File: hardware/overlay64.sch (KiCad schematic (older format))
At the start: 16 parts, among them IC1 ATMEGA328P-P, P1 ISP, P2 MAIN, P3 INPUT, Q1 BC547, U1 LM1881, Y1 20MHz

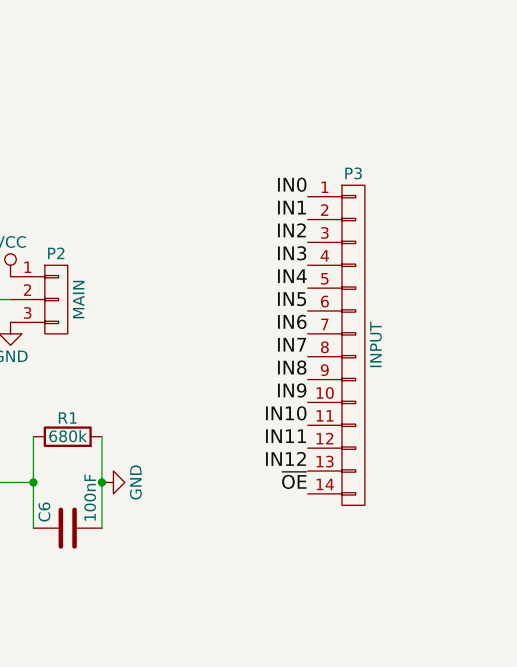
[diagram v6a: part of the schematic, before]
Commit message: Hardware: Added dual 14 pin header for bypassing the inputs
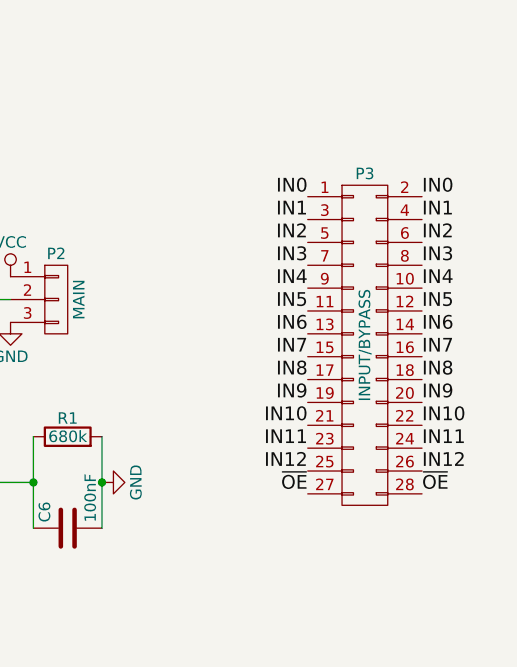
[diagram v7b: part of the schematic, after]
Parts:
- removed P3: INPUT, Pin_Headers:Pin_Header_Straight_1x14, symbol CONN_01X14
- added P3: INPUT/BYPASS, Pin_Headers:Pin_Header_Straight_2x14, symbol CONN_02X14
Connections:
- net IN0: now also P3.1 (P1), P3.2 (P2)
- net IN1: now also P3.3 (P3), P3.4 (P4)
- net IN10: now also P3.21 (P21), P3.22 (P22)
- net IN11: now also P3.23 (P23), P3.24 (P24)
- net IN12: now also P3.25 (P25), P3.26 (P26)
- net IN2: now also P3.5 (P5), P3.6 (P6)
- net IN3: now also P3.7 (P7), P3.8 (P8)
- net IN4: now also P3.10 (P10), P3.9 (P9)
- net IN5: now also P3.11 (P11), P3.12 (P12)
- net IN6: now also P3.13 (P13), P3.14 (P14)
- net IN7: now also P3.15 (P15), P3.16 (P16)
- net IN8: now also P3.17 (P17), P3.18 (P18)
- net IN9: now also P3.19 (P19), P3.20 (P20)
- net ~OE: now also P3.27 (P27), P3.28 (P28)
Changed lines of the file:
@@
 $EndComp
 $Comp
-L PWR_FLAG #FLG1
+L PWR_FLAG #FLG01
 U 1 1 56A1EF0B
 P 6250 7500
-F 0 "#FLG1" H 6250 7595 50  0001 C CNN
+F 0 "#FLG01" H 6250 7595 50  0001 C CNN
 F 1 "PWR_FLAG" H 6250 7680 50  0000 C CNN
 F 2 "" H 6250 7500 60  0000 C CNN
@@
 $EndComp
 $Comp
-L VCC #PWR12
+L VCC #PWR02
 U 1 1 56A1EF40
 P 6250 7500
-F 0 "#PWR12" H 6250 7350 50  0001 C CNN
+F 0 "#PWR02" H 6250 7350 50  0001 C CNN
 F 1 "VCC" H 6250 7650 50  0000 C CNN
 F 2 "" H 6250 7500 60  0000 C CNN
@@
 $EndComp
 $Comp
-L PWR_FLAG #FLG2
+L PWR_FLAG #FLG03
 U 1 1 56A1EF56
 P 6700 7500
-F 0 "#FLG2" H 6700 7595 50  0001 C CNN
+F 0 "#FLG03" H 6700 7595 50  0001 C CNN
 F 1 "PWR_FLAG" H 6700 7680 50  0000 C CNN
 F 2 "" H 6700 7500 60  0000 C CNN
@@
 $EndComp
 $Comp
-L GND #PWR15
+L GND #PWR04
 U 1 1 56A1EF6C
 P 6700 7500
-F 0 "#PWR15" H 6700 7250 50  0001 C CNN
+F 0 "#PWR04" H 6700 7250 50  0001 C CNN
 F 1 "GND" H 6700 7350 50  0000 C CNN
 F 2 "" H 6700 7500 60  0000 C CNN
@@
 $EndComp
 $Comp
-L VCC #PWR9
+L VCC #PWR05
 U 1 1 56A1F13D
 P 5600 4850
-F 0 "#PWR9" H 5600 4700 50  0001 C CNN
+F 0 "#PWR05" H 5600 4700 50  0001 C CNN
 F 1 "VCC" H 5600 5000 50  0000 C CNN
 F 2 "" H 5600 4850 60  0000 C CNN
@@
 $EndComp
 $Comp
-L GND #PWR10
+L GND #PWR06
 U 1 1 56A1F155
 P 5600 5150
-F 0 "#PWR10" H 5600 4900 50  0001 C CNN
+F 0 "#PWR06" H 5600 4900 50  0001 C CNN
 F 1 "GND" H 5600 5000 50  0000 C CNN
 F 2 "" H 5600 5150 60  0000 C CNN
@@
 $EndComp
 $Comp
-L GND #PWR2
+L GND #PWR07
 U 1 1 56A1F1BC
 P 2050 2800
-F 0 "#PWR2" H 2050 2550 50  0001 C CNN
+F 0 "#PWR07" H 2050 2550 50  0001 C CNN
 F 1 "GND" H 2050 2650 50  0000 C CNN
 F 2 "" H 2050 2800 60  0000 C CNN
@@
 $EndComp
 $Comp
-L GND #PWR16
+L GND #PWR08
 U 1 1 56A1F3BB
 P 6850 4350
-F 0 "#PWR16" H 6850 4100 50  0001 C CNN
+F 0 "#PWR08" H 6850 4100 50  0001 C CNN
 F 1 "GND" H 6850 4200 50  0000 C CNN
 F 2 "" H 6850 4350 60  0000 C CNN
@@
 $EndComp
 $Comp
-L VCC #PWR1
+L VCC #PWR09
 U 1 1 56A1FF3A
 P 2000 2500
-F 0 "#PWR1" H 2000 2350 50  0001 C CNN
+F 0 "#PWR09" H 2000 2350 50  0001 C CNN
 F 1 "VCC" H 2000 2650 50  0000 C CNN
 F 2 "" H 2000 2500 60  0000 C CNN
@@
 $EndComp
 $Comp
-L GND #PWR3
+L GND #PWR010
 U 1 1 56A20155
 P 2450 4700
-F 0 "#PWR3" H 2450 4450 50  0001 C CNN
+F 0 "#PWR010" H 2450 4450 50  0001 C CNN
 F 1 "GND" H 2450 4550 50  0000 C CNN
 F 2 "" H 2450 4700 60  0000 C CNN
@@
 $EndComp
 $Comp
-L GND #PWR4
+L GND #PWR011
 U 1 1 56A60DBD
 P 2450 4800
-F 0 "#PWR4" H 2450 4550 50  0001 C CNN
+F 0 "#PWR011" H 2450 4550 50  0001 C CNN
 F 1 "GND" H 2450 4650 50  0000 C CNN
 F 2 "" H 2450 4800 60  0000 C CNN
@@
 $EndComp
 $Comp
-L VCC #PWR11
+L VCC #PWR012
 U 1 1 56A78618
 P 5800 2600
-F 0 "#PWR11" H 5800 2450 50  0001 C CNN
+F 0 "#PWR012" H 5800 2450 50  0001 C CNN
 F 1 "VCC" H 5800 2750 50  0000 C CNN
 F 2 "" H 5800 2600 60  0000 C CNN
@@
 MOSI
 $Comp
-L VCC #PWR5
+L VCC #PWR013
 U 1 1 56A92B5A
 P 3750 1750
-F 0 "#PWR5" H 3750 1600 50  0001 C CNN
+F 0 "#PWR013" H 3750 1600 50  0001 C CNN
 F 1 "VCC" H 3750 1900 50  0000 C CNN
 F 2 "" H 3750 1750 60  0000 C CNN
@@
 $EndComp
 $Comp
-L GND #PWR6
+L GND #PWR014
 U 1 1 56A92BBD
 P 3750 1950
-F 0 "#PWR6" H 3750 1700 50  0001 C CNN
+F 0 "#PWR014" H 3750 1700 50  0001 C CNN
 F 1 "GND" H 3750 1800 50  0000 C CNN
 F 2 "" H 3750 1950 60  0000 C CNN
@@
 $EndComp
 $Comp
-L GND #PWR7
+L GND #PWR015
 U 1 1 56A976F1
 P 4850 3050
-F 0 "#PWR7" H 4850 2800 50  0001 C CNN
+F 0 "#PWR015" H 4850 2800 50  0001 C CNN
 F 1 "GND" H 4850 2900 50  0000 C CNN
 F 2 "" H 4850 3050 60  0000 C CNN
@@
 $EndComp
 $Comp
-L GND #PWR8
+L GND #PWR016
 U 1 1 56A97733
 P 4850 3250
-F 0 "#PWR8" H 4850 3000 50  0001 C CNN
+F 0 "#PWR016" H 4850 3000 50  0001 C CNN
 F 1 "GND" H 4850 3100 50  0000 C CNN
 F 2 "" H 4850 3250 60  0000 C CNN
@@
 $EndComp
 $Comp
-L VCC #PWR13
+L VCC #PWR017
 U 1 1 56A9E7D0
 P 6450 3450
-F 0 "#PWR13" H 6450 3300 50  0001 C CNN
+F 0 "#PWR017" H 6450 3300 50  0001 C CNN
 F 1 "VCC" H 6450 3600 50  0000 C CNN
 F 2 "" H 6450 3450 60  0000 C CNN
@@
 $EndComp
 $Comp
-L GND #PWR14
+L GND #PWR018
 U 1 1 56A9E875
 P 6450 3650
-F 0 "#PWR14" H 6450 3400 50  0001 C CNN
+F 0 "#PWR018" H 6450 3400 50  0001 C CNN
 F 1 "GND" H 6450 3500 50  0000 C CNN
 F 2 "" H 6450 3650 60  0000 C CNN
@@
 Wire Wire Line
 	4750 4450 5300 4450
-$Comp
-L CONN_01X14 P3
-U 1 1 56A9F1EA
-P 7950 3750
-F 0 "P3" H 7950 4500 50  0000 C CNN
-F 1 "INPUT" V 8050 3750 50  0000 C CNN
-F 2 "Pin_Headers:Pin_Header_Straight_1x14" H 7950 3750 60  0001 C CNN
-F 3 "" H 7950 3750 60  0000 C CNN
-	1    7950 3750
-	1    0    0    -1
-$EndComp
 Text Label 7750 3100 2    60   ~ 0
 IN0
@@
 Text Label 6150 3550 0    60   ~ 0
 LUMA
+$Comp
+L CONN_02X14 P3
+U 1 1 56B0DCD2
+P 8000 3750
+F 0 "P3" H 8000 4500 50  0000 C CNN
+F 1 "INPUT/BYPASS" V 8000 3750 50  0000 C CNN
+F 2 "Pin_Headers:Pin_Header_Straight_2x14" H 8000 2600 60  0001 C CNN
+F 3 "" H 8000 2600 60  0000 C CNN
+	1    8000 3750
+	1    0    0    -1
+$EndComp
+Text Label 8250 4400 0    60   ~ 0
+~OE
+Text Label 8250 3100 0    60   ~ 0
+IN0
+Text Label 8250 3200 0    60   ~ 0
+IN1
+Text Label 8250 3300 0    60   ~ 0
+IN2
+Text Label 8250 3400 0    60   ~ 0
+IN3
+Text Label 8250 3500 0    60   ~ 0
+IN4
+Text Label 8250 3600 0    60   ~ 0
+IN5
+Text Label 8250 3700 0    60   ~ 0
+IN6
+Text Label 8250 3800 0    60   ~ 0
+IN7
+Text Label 8250 3900 0    60   ~ 0
+IN8
+Text Label 8250 4000 0    60   ~ 0
+IN9
+Text Label 8250 4100 0    60   ~ 0
+IN10
+Text Label 8250 4200 0    60   ~ 0
+IN11
+Text Label 8250 4300 0    60   ~ 0
+IN12
 $EndSCHEMATC

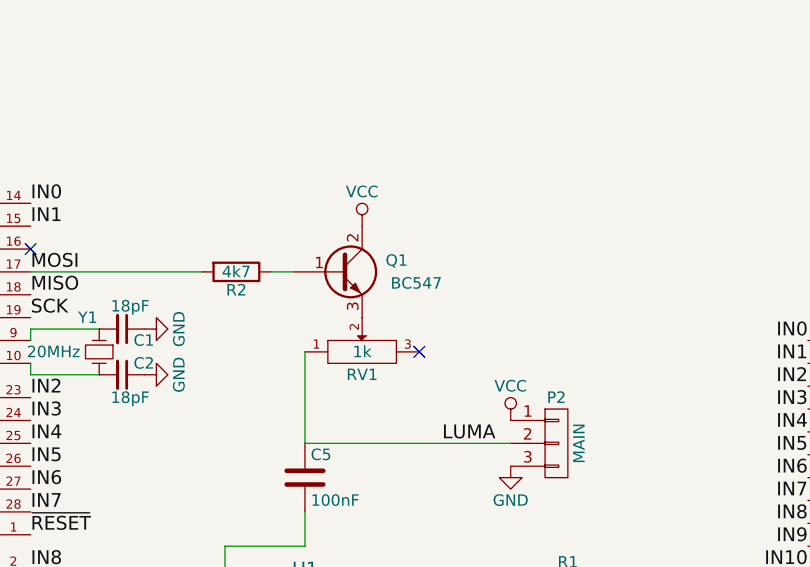
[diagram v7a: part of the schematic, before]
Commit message: Hardware: Specified correct transistor type (BC547B)
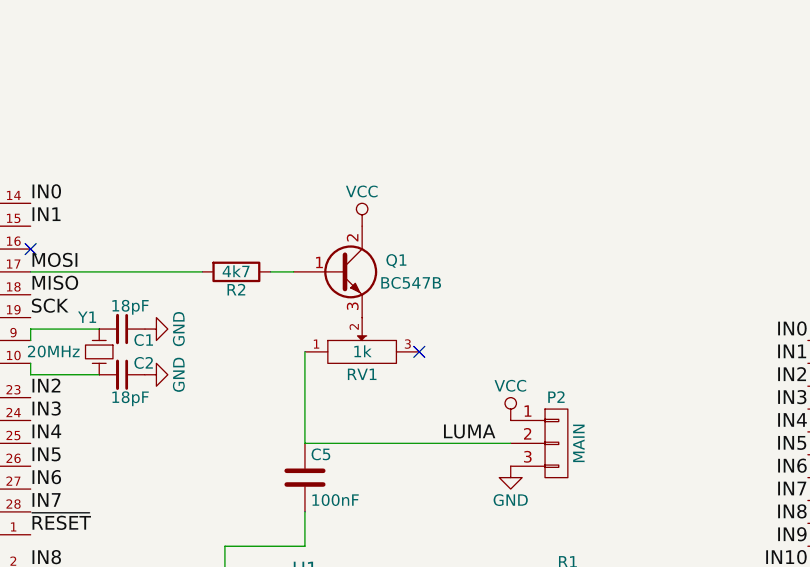
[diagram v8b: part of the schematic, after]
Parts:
- Q1: value BC547 -> BC547B
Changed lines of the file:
@@
 P 5700 2800
 F 0 "Q1" H 6000 2850 50  0000 R CNN
-F 1 "BC547" H 6150 2750 50  0000 R CNN
+F 1 "BC547B" H 6150 2750 50  0000 R CNN
 F 2 "TO_SOT_Packages_THT:TO-92_Inline_Narrow_Oval" H 5900 2900 29  0001 C CNN
 F 3 "" H 5700 2800 60  0000 C CNN
